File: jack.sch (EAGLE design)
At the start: 28 parts, among them IC1 NUF2221W1T2G, IC2 ATSAMD21G18, IC3 LDO, SW1 SPST, X1 TSX-3225 24.0000MF10Z-C3

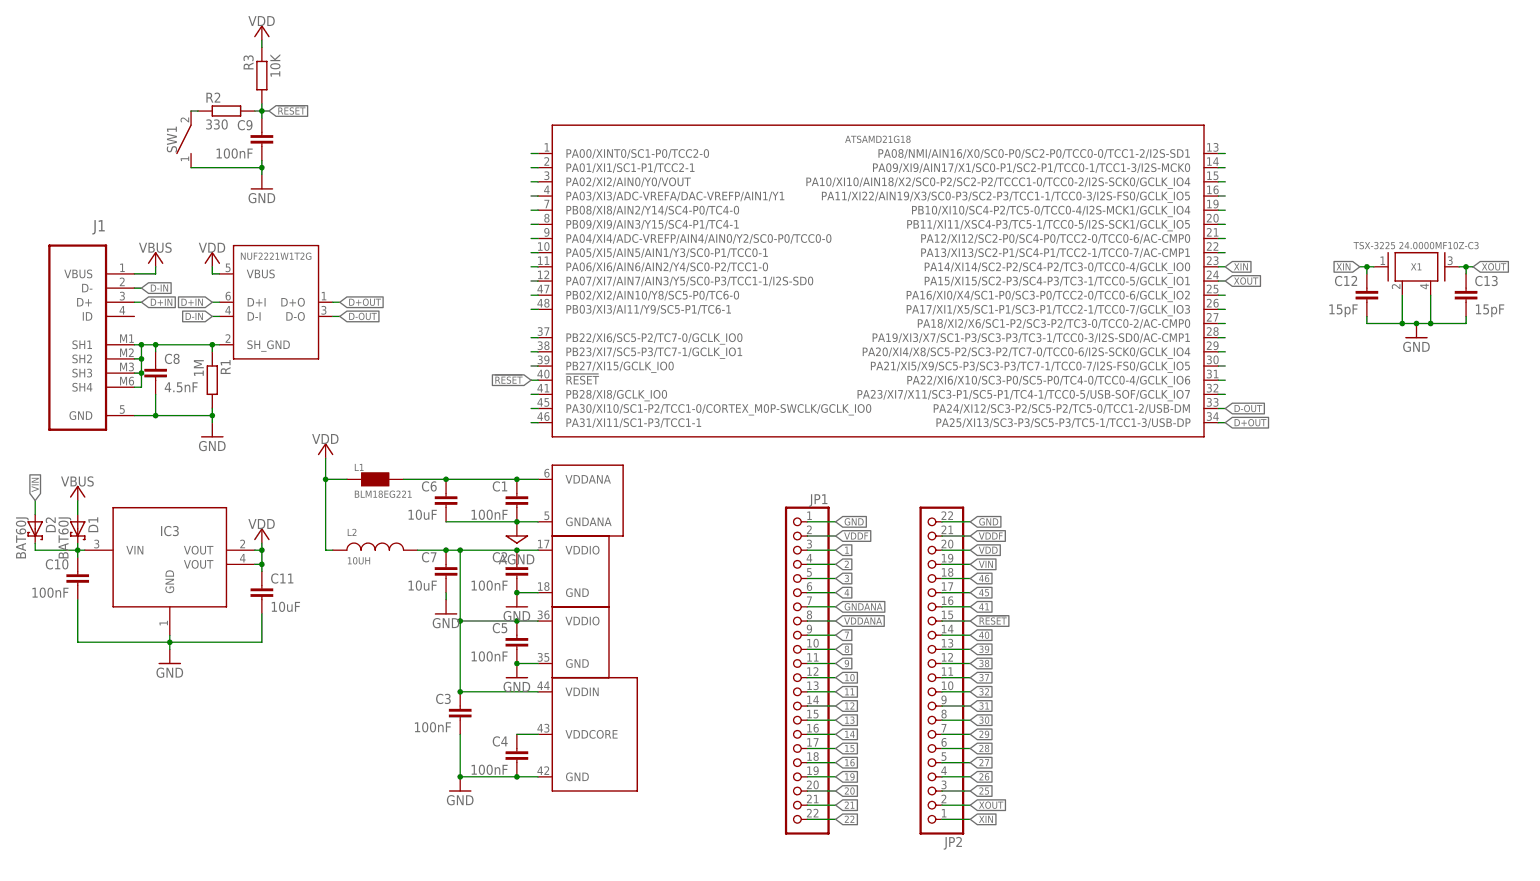
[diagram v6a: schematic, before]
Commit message: :hatching_chick: Polished schematic, started layout
I polished the schematic so to let people easily understand what does
what, dividing it in sections with a description; I did a hi-res picture
of it so to see it without having to open Eagle CAD; also, I started the
layout process; you can already see on the PCB where stuff should go in
the end
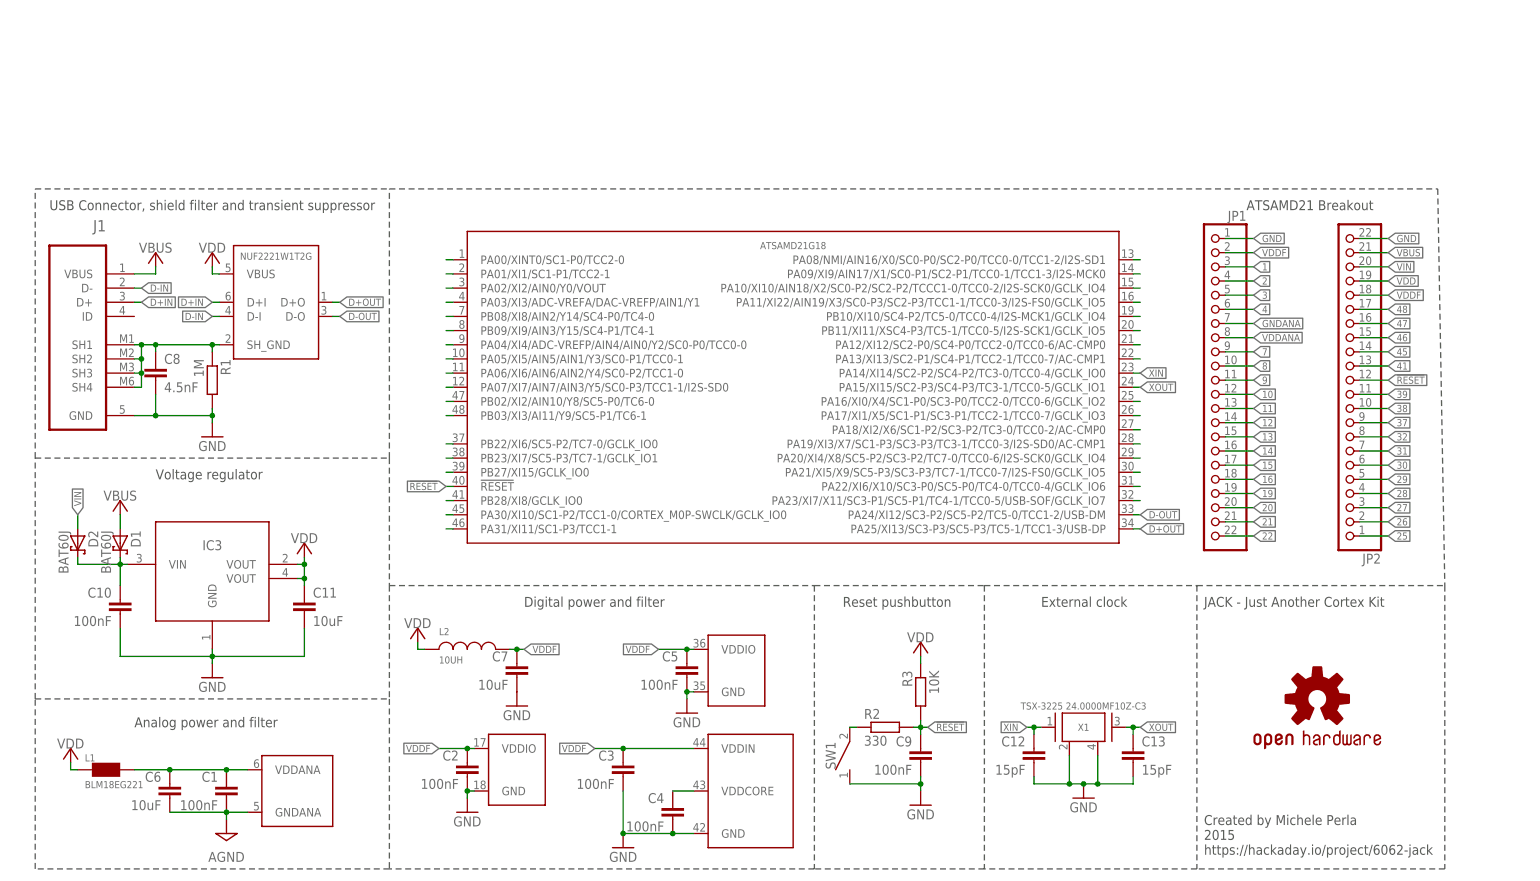
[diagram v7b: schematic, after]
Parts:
- added LOGO1: OSHW-LOGOL, SparkFun-Aesthetics:OSHW-LOGOL
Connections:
- removed net 40: JP2.14
- removed net AGND: C1.2, C6.2, IC2PWR-ANA.GNDANA
- net !RESET: now also JP2.12; no longer JP2.15
- net 25: now also JP2.1; no longer JP2.3
- net 26: now also JP2.2; no longer JP2.4
- net 27: now also JP2.3; no longer JP2.5
- net 28: now also JP2.4; no longer JP2.6
- net 29: now also JP2.5; no longer JP2.7
- net 30: now also JP2.6; no longer JP2.8
- net 31: now also JP2.7; no longer JP2.9
- net 32: now also JP2.8; no longer JP2.10
- net 37: now also JP2.9; no longer JP2.11
- net 38: now also JP2.10; no longer JP2.12
- net 39: now also JP2.11; no longer JP2.13
- net 41: now also JP2.13; no longer JP2.16
- net 45: now also JP2.14; no longer JP2.17
- net 46: now also JP2.15; no longer JP2.18
- net 47: now also JP2.16
- net 48: now also JP2.17
- net GNDANA: now also C1.2, C6.2, IC2PWR-ANA.GNDANA
- net VBUS: now also JP2.21
- net VDD: now also JP2.19; no longer JP2.20
- net VDDF: now also JP2.18; no longer JP2.21
- net VIN: now also JP2.20; no longer JP2.19
- net XIN: no longer JP2.1
- net XOUT: no longer JP2.2
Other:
- note added: "ATSAMD21 Breakout"
- note added: "Analog power and filter"
- note added: "Created by Michele Perla 2015 https://hackaday.io/project/6062-jack"
- note added: "Digital power and filter"
- note added: "External clock"
- note added: "JACK - Just Another Cortex Kit"
- note added: "Reset pushbutton"
- note added: "USB Connector, shield filter and transient suppressor"
- note added: "Voltage regulator"
- moved on the sheet: C1, C10, C11, C12, C13, C2, C3, C4, C5, C6, C7, C9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

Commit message: :wavy_dash: Progressing with layout
Still dealing with layout, in particular dealing with analog/digital
power, decoupling caps and correct power grounding (one ground to rule
them all, or local a/d planes near chip and then star ground near LDO?)
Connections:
- net N$2 renamed LDOIN
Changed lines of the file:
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@@
 </segment>
 </net>
-<net name="N$2" class="0">
+<net name="LDOIN" class="0">
 <segment>
 <pinref part="C10" gate="G$1" pin="1"/>
